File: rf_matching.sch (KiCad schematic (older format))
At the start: 12 parts, among them J1 RFI, J2 RFO, J3 CTRL, J4 ANT, J5 3V3, U1 pe4259ds, U2 SF2098

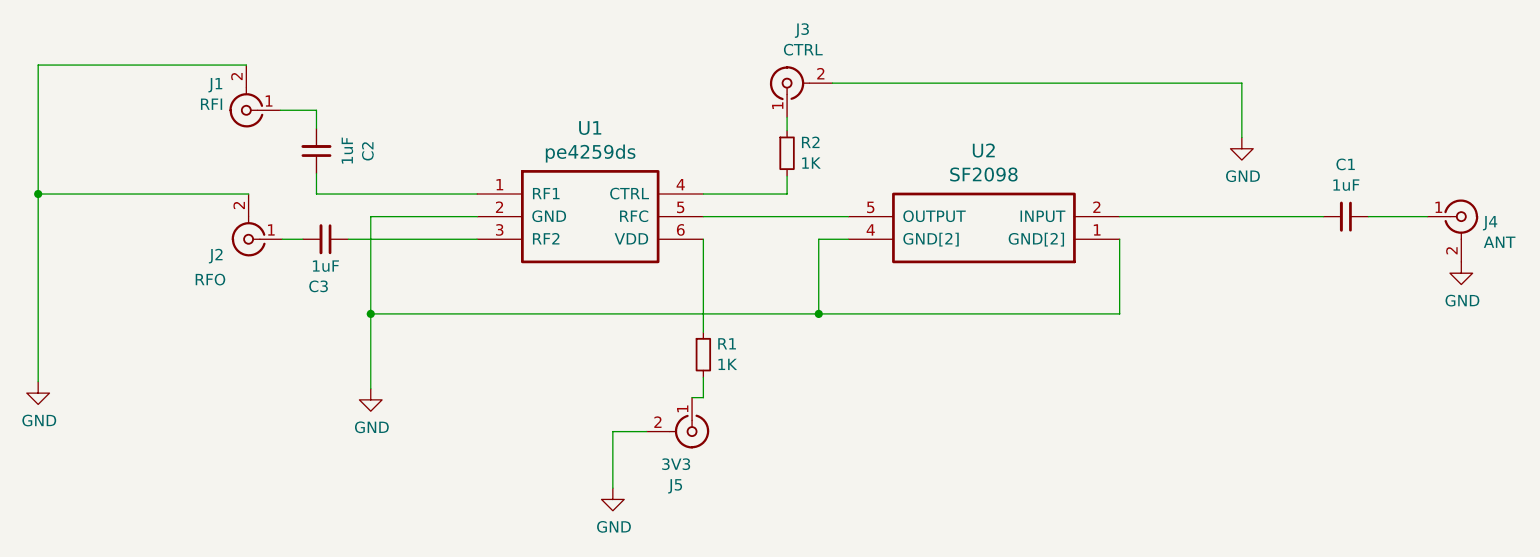
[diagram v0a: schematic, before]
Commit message: RF switch only branch
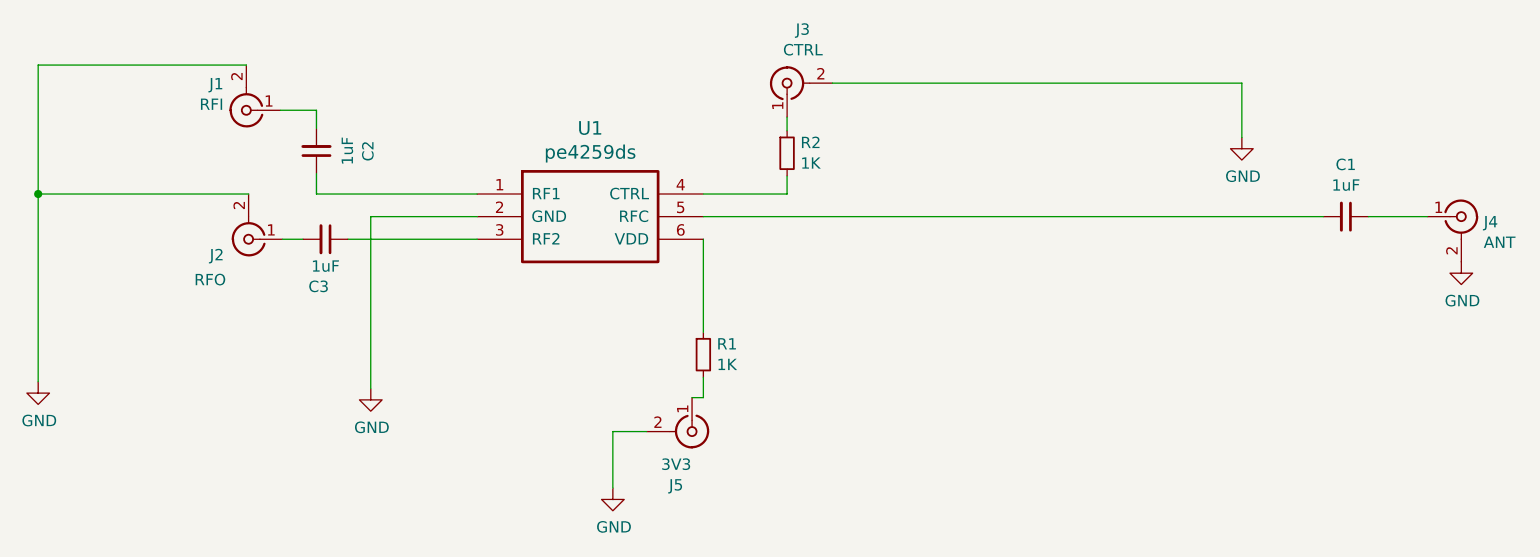
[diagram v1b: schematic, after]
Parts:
- removed U2: SF2098, SON120P300X300X110-6N:SON120P300X300X110-6N, symbol SF2098
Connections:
- net at C1.2: now also U1.5 (RFC)
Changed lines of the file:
@@
 $EndDescr
-$Comp
-L SF2098 U2
-U 1 1 5B4ACEE6
-P 6870 4250
-F 0 "U2" H 7470 3860 60  0000 C CNN
-F 1 "SF2098" H 7470 3966 60  0000 C CNN
-F 2 "SON120P300X300X110-6N:SON120P300X300X110-6N" H 6870 4250 60  0001 C CNN
-F 3 "" H 6870 4250 60  0001 C CNN
-	1    6870 4250
-	-1   0    0    1
-$EndComp
 $Comp
 L Conn_Coaxial J1
@@
 $EndComp
 Wire Wire Line
-	5670 4150 5030 4150
+	5030 4150 7770 4150
 Wire Wire Line
 	4030 4150 3560 4150
@@
 	3010 3480 2090 3480
 Connection ~ 2090 4050
-Wire Wire Line
-	6870 4580 6870 4250
-Wire Wire Line
-	3560 4580 6870 4580
-Connection ~ 3560 4580
-Wire Wire Line
-	5670 4250 5540 4250
-Wire Wire Line
-	5540 4250 5540 4580
-Connection ~ 5540 4580
 Wire Wire Line
 	5030 4050 5400 4050
@@
 Wire Wire Line
 	8230 4150 7970 4150
-Wire Wire Line
-	7770 4150 6870 4150
 $Comp
 L C_Small C2
